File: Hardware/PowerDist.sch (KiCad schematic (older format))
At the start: 9 parts, among them SW1 SPST, U1 LM7805

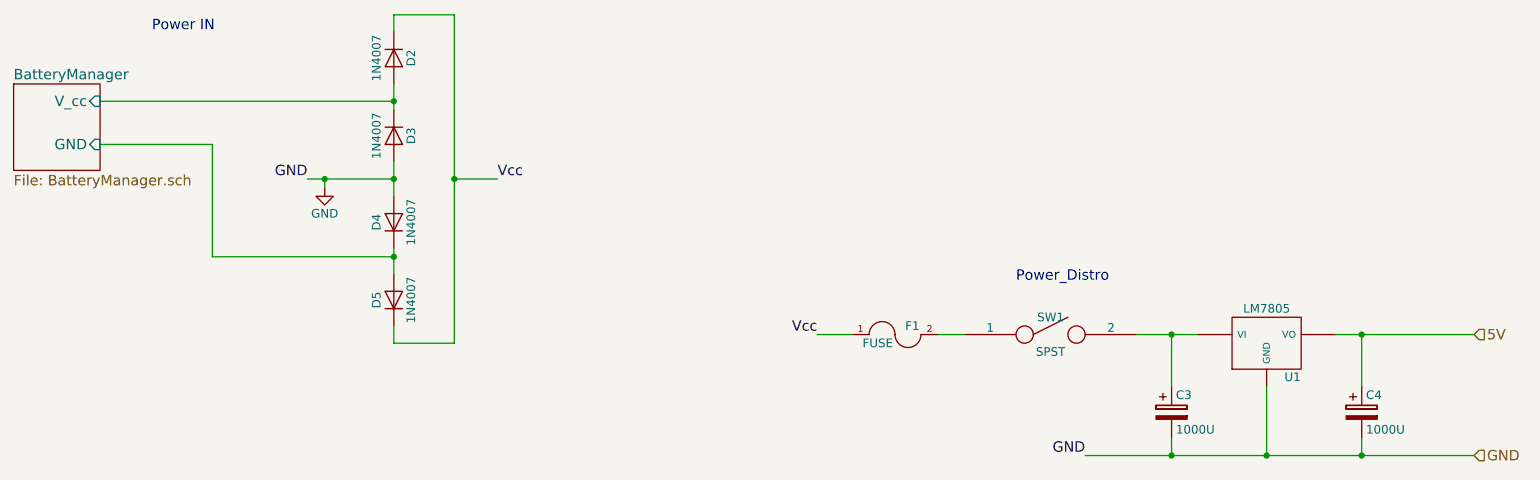
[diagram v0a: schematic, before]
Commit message: Add receiver component
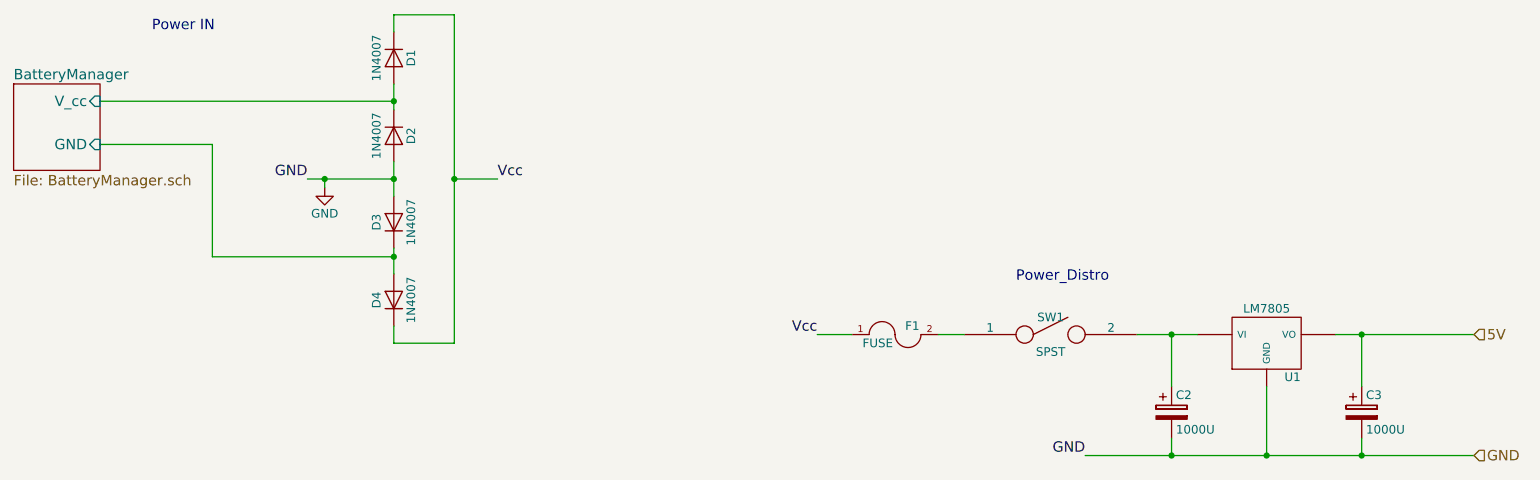
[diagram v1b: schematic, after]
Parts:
- renumbered C3 to C2, C4 to C3, D2 to D1, D3 to D2, D4 to D3, D5 to D4
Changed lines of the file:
@@
 LIBS:valves
 LIBS:arduino
-LIBS:RC_Car_Manager-cache
+LIBS:RC_CAR
 EELAYER 25 0
 EELAYER END
@@
 $EndComp
 $Comp
-L CP C3
+L CP C2
 U 1 1 5A341BEC
 P 8000 3600
-F 0 "C3" H 8025 3700 50  0000 L CNN
+F 0 "C2" H 8025 3700 50  0000 L CNN
 F 1 "1000U" H 8025 3500 50  0000 L CNN
 F 2 "" H 8038 3450 50  0000 C CNN
@@
 $EndComp
 $Comp
-L CP C4
+L CP C3
 U 1 1 5A341BF3
 P 9100 3600
-F 0 "C4" H 9125 3700 50  0000 L CNN
+F 0 "C3" H 9125 3700 50  0000 L CNN
 F 1 "1000U" H 9125 3500 50  0000 L CNN
 F 2 "" H 9138 3450 50  0000 C CNN
@@
 	1800 1800 3500 1800
 $Comp
-L D D2
+L D D1
 U 1 1 5A34221E
 P 3500 1550
-F 0 "D2" H 3500 1650 50  0000 C CNN
+F 0 "D1" H 3500 1650 50  0000 C CNN
 F 1 "1N4007" H 3500 1450 50  0000 C CNN
 F 2 "" H 3500 1550 50  0000 C CNN
@@
 $EndComp
 $Comp
-L D D3
+L D D2
 U 1 1 5A34226F
 P 3500 2000
-F 0 "D3" H 3500 2100 50  0000 C CNN
+F 0 "D2" H 3500 2100 50  0000 C CNN
 F 1 "1N4007" H 3500 1900 50  0000 C CNN
 F 2 "" H 3500 2000 50  0000 C CNN
@@
 Connection ~ 3500 1800
 $Comp
-L D D4
+L D D3
 U 1 1 5A34240E
 P 3500 2500
-F 0 "D4" H 3500 2600 50  0000 C CNN
+F 0 "D3" H 3500 2600 50  0000 C CNN
 F 1 "1N4007" H 3500 2400 50  0000 C CNN
 F 2 "" H 3500 2500 50  0000 C CNN
@@
 $EndComp
 $Comp
-L D D5
+L D D4
 U 1 1 5A342490
 P 3500 2950
-F 0 "D5" H 3500 3050 50  0000 C CNN
+F 0 "D4" H 3500 3050 50  0000 C CNN
 F 1 "1N4007" H 3500 2850 50  0000 C CNN
 F 2 "" H 3500 2950 50  0000 C CNN
@@
 	3000 2250 3500 2250
 $Comp
-L GND #PWR10
+L GND #PWR6
 U 1 1 5A3438CD
 P 3100 2300
-F 0 "#PWR10" H 3100 2050 50  0001 C CNN
+F 0 "#PWR6" H 3100 2050 50  0001 C CNN
 F 1 "GND" H 3100 2150 50  0000 C CNN
 F 2 "" H 3100 2300 50  0000 C CNN
